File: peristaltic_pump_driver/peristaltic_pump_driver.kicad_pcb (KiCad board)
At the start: 4 copper layers, 6 parts, among them M1 Motor_DC, Q1 BUZ31H3046

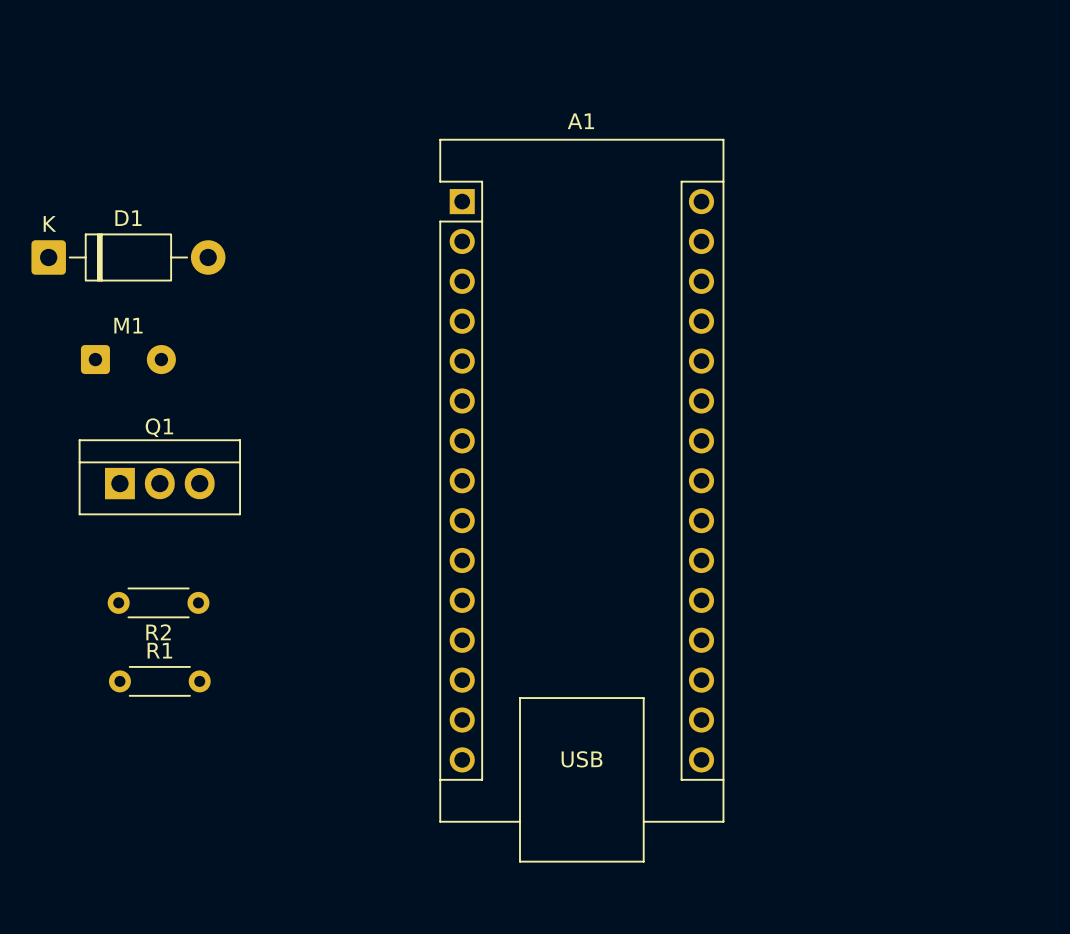
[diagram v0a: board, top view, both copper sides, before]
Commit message: pcb design v2 traces done
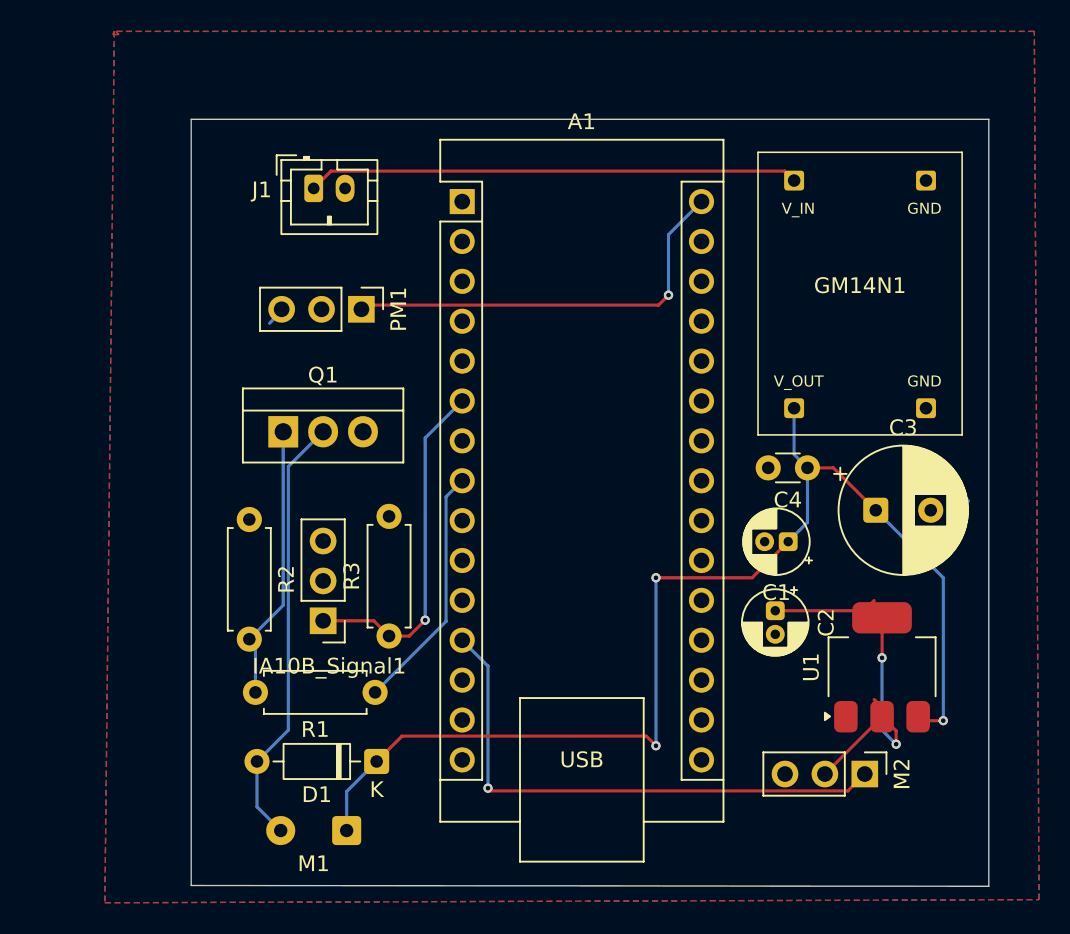
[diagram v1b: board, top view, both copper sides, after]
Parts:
- added C1: 10u, Capacitor_THT:CP_Radial_D4.0mm_P1.50mm, F.Cu at (126.0, 110.6)
- added C2: 10u, Capacitor_THT:CP_Radial_D4.0mm_P1.50mm, F.Cu at (125.2, 115.0)
- added C3: 100u, Capacitor_THT:CP_Radial_D8.0mm_P3.50mm, F.Cu at (131.6, 108.6)
- added C4: 100n, Capacitor_THT:C_Disc_D3.0mm_W1.6mm_P2.50mm, F.Cu at (127.2, 105.9)
- added GM14N1: Buck, entropy_footprints:Untitled_1, F.Cu at (130.6, 94.8)
- added IA10B_Signal1: ~, Connector_PinHeader_2.54mm:PinHeader_1x03_P2.54mm_Vertical, F.Cu at (96.4, 115.6)
- added J1: Conn_01x02_Socket, Connector_JST:JST_PH_B2B-PH-K_1x02_P2.00mm_Vertical, F.Cu at (95.8, 88.1)
- added M2: MG90S_Servo, Connector_PinHeader_2.54mm:PinHeader_1x03_P2.54mm_Vertical, F.Cu at (130.9, 125.4)
- added PM1: Buck, Connector_PinHeader_2.54mm:PinHeader_1x03_P2.54mm_Vertical, F.Cu at (98.8, 95.8)
- added R3: 10k, Resistor_THT:R_Axial_DIN0207_L6.3mm_D2.5mm_P7.62mm_Horizontal, F.Cu at (100.6, 116.6)
- added U1: AMS1117-3.3, Package_TO_SOT_SMD:SOT-223-3_TabPin2, F.Cu at (132.0, 118.6)
- D1: footprint Diode_THT:D_DO-41_SOD81_P10.16mm_Horizontal -> Diode_THT:D_DO-35_SOD27_P7.62mm_Horizontal
- M1: value Motor_DC -> Pump
- R1: footprint Resistor_THT:R_Axial_DIN0204_L3.6mm_D1.6mm_P5.08mm_Horizontal -> Resistor_THT:R_Axial_DIN0207_L6.3mm_D2.5mm_P7.62mm_Horizontal
- R2: value 9.76k -> 10k; footprint Resistor_THT:R_Axial_DIN0204_L3.6mm_D1.6mm_P5.08mm_Horizontal -> Resistor_THT:R_Axial_DIN0207_L6.3mm_D2.5mm_P7.62mm_Horizontal
- moved D1 38.3 mm to (99.8, 124.6), turned to 180 degrees
- moved M1 34.0 mm to (97.9, 129.0), turned to 180 degrees
- moved R1 16.3 mm to (99.7, 120.2), turned to 180 degrees
- moved Q1 10.9 mm to (93.9, 103.6)
- moved R2 6.22 mm to (91.7, 109.2), turned to -90 degrees
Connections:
- net +12V renamed Net-(D1-K)
- A1 pad 12: unconnected-(A1-D9-Pad12) -> Net-(A1-D9)
- A1 pad 13: Net-(A1-D10) -> unconnected-(A1-D10-Pad13)
- A1 pad 29: unconnected-(A1-GND-Pad29) -> GND
- A1 pad 30: unconnected-(A1-VIN-Pad30) -> Net-(A1-VIN)
- A1 pad 4: unconnected-(A1-GND-Pad4) -> GND
- A1 pad 6: unconnected-(A1-D3-Pad6) -> Net-(A1-D3)
- A1 pad 8: unconnected-(A1-D5-Pad8) -> Net-(A1-D5)
- R1 pad 1: Net-(A1-D10) -> Net-(A1-D5)
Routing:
- net Net-(D1-K): track 0.00 -> 75.7 mm, vias 0 -> 3
- net Net-(A1-D9): track 0.00 -> 34.6 mm, vias 0 -> 1
- net Net-(GM14N1-V_IN): track 0.00 -> 31.3 mm
- net Net-(D1-A): track 0.00 -> 27.8 mm
- net Net-(A1-VIN): track 0.00 -> 26.8 mm, vias 0 -> 1
- net Net-(M2-+): track 0.00 -> 25.6 mm, vias 0 -> 2
- net Net-(A1-D3): track 0.00 -> 22.3 mm, vias 0 -> 1
- net Net-(Q1-G): track 0.00 -> 17.7 mm
- net Net-(A1-D5): track 0.00 -> 15.8 mm
- net GND: track 0.00 -> 1.17 mm
- added copper zone on B.Cu, net GND
- added copper zone on F.Cu, net GND
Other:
- board outline added: 50.8 x 48.9 mm
